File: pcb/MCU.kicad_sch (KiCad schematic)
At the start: 22 parts, among them J2 TC2030, J3 Conn_01x02_Pin, U6 FM24C64B, U7 STM32H563VITx, Y1 3225-25M-SR

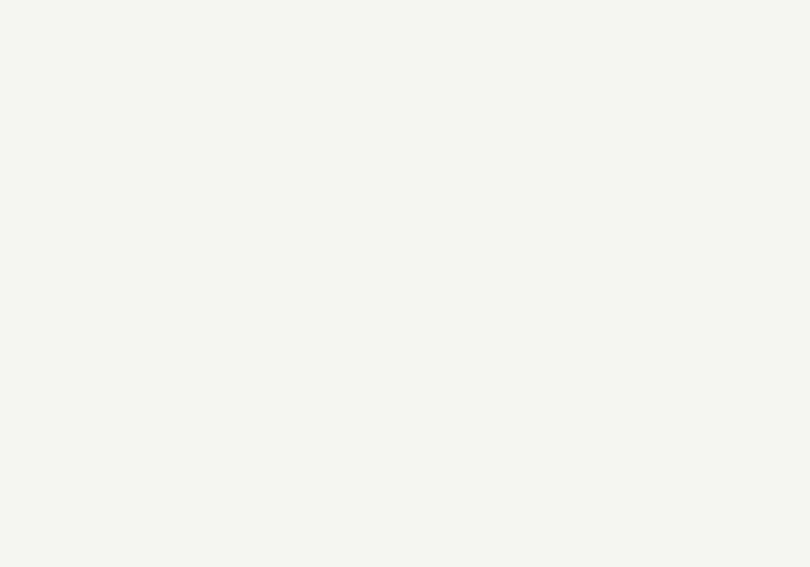
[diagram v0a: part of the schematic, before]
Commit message: Add UniConnector for io expansion (2.0mm pinheader)
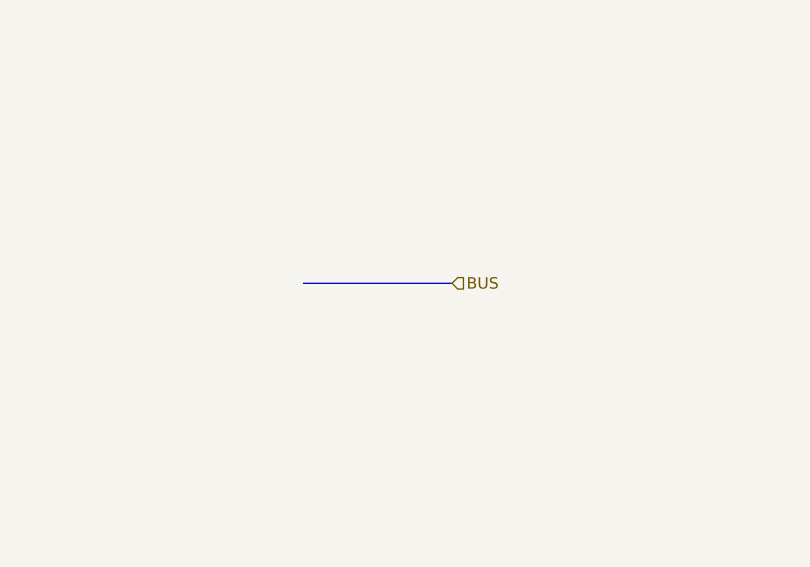
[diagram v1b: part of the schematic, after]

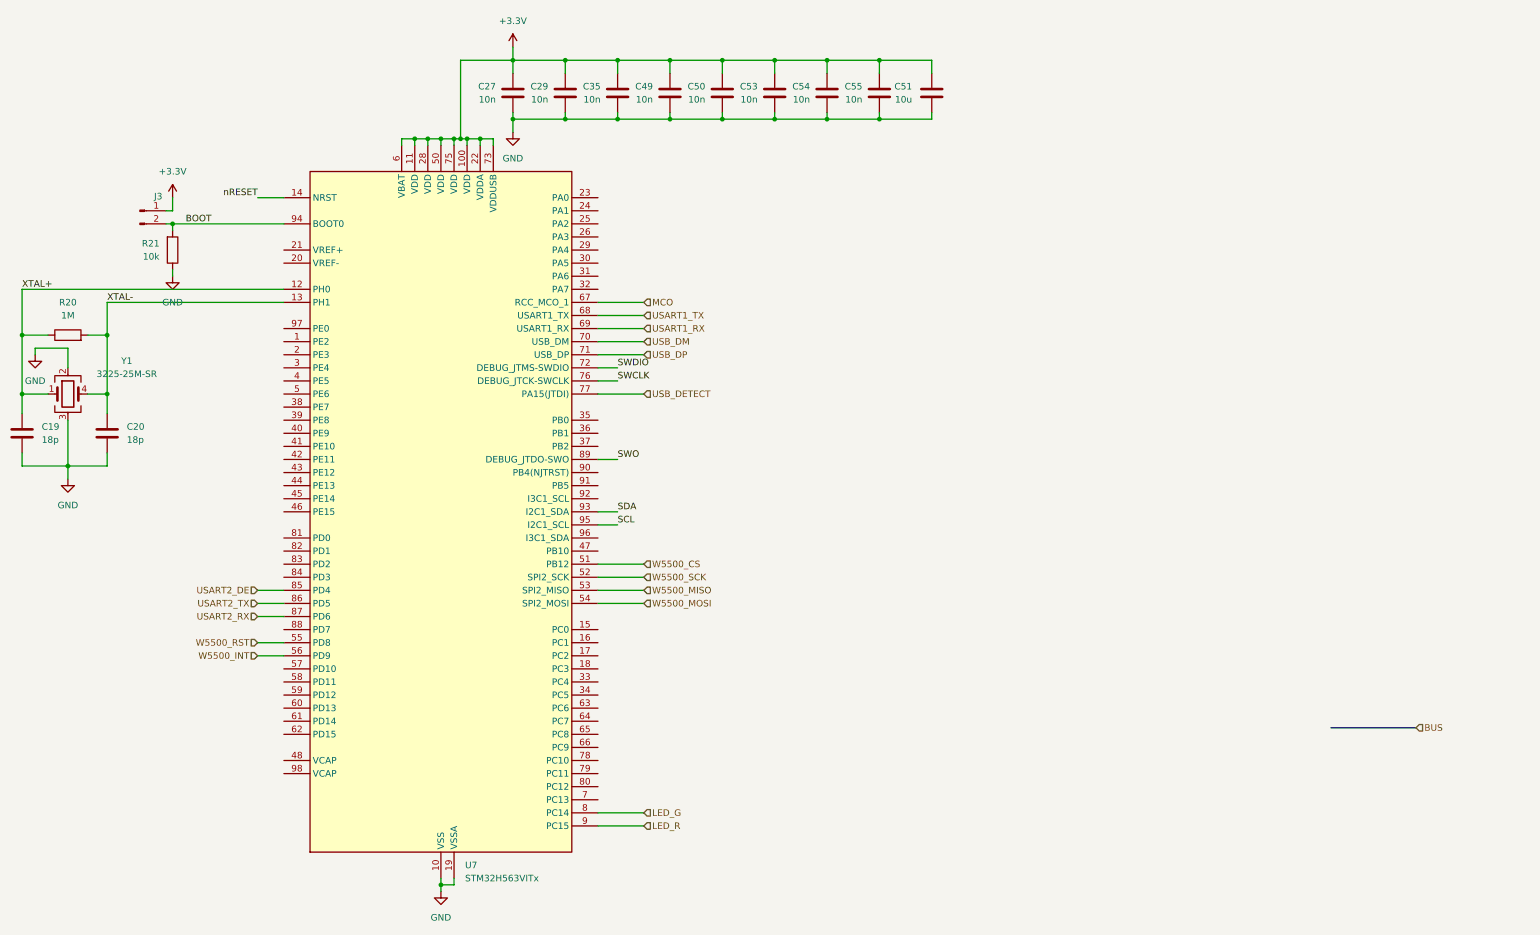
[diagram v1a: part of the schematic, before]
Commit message: Add junction and bus entries to UniConnector schematic
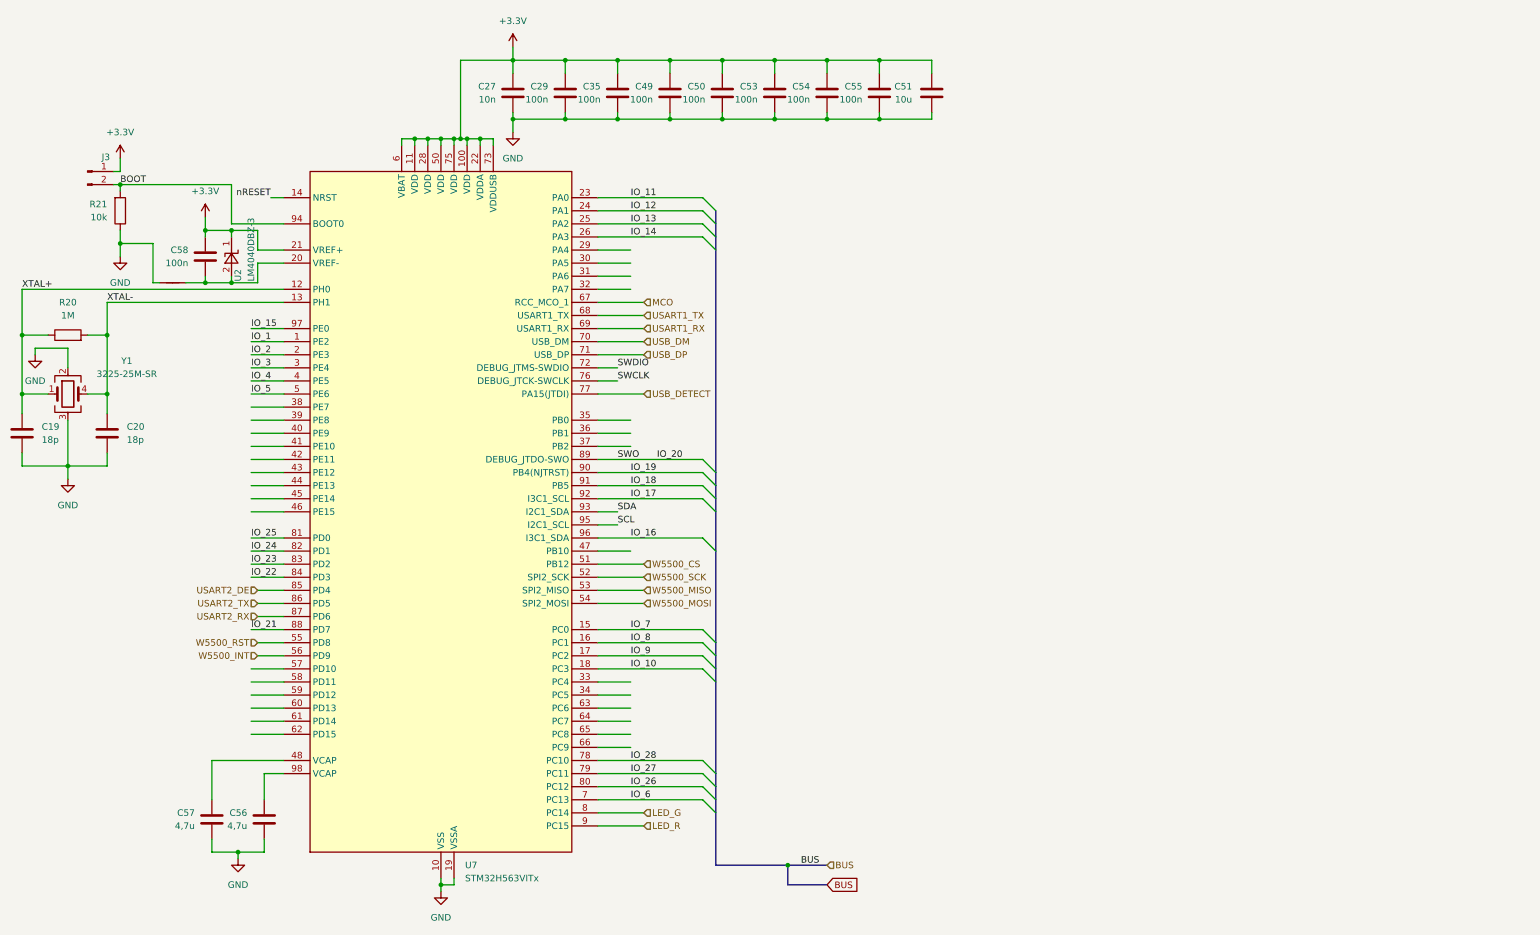
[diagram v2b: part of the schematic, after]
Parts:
- added C56, C57: 4,7u, Capacitor_SMD:C_0603_1608Metric_Pad1.08x0.95mm_HandSolder, symbol Device:C
- added C58: 100n, Capacitor_SMD:C_0603_1608Metric_Pad1.08x0.95mm_HandSolder, symbol Device:C
- added NT1: NetTie_2, NetTie:NetTie-2_SMD_Pad0.5mm, symbol Device:NetTie_2
- added U2: LM4040DBZ-3, Package_TO_SOT_SMD:SOT-23_Handsoldering, symbol Reference_Voltage:LM4040DBZ-3
- C29, C35, C49, C50, C53, C54, C55: value 10n -> 100n
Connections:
- net +3.3V: now also U7.21 (VREF+), C58.2, U2.1 (K)
- net GND: now also C56.1, C57.1, NT1.1
- net IO_1: now reaches U7.1 (PE2)
- net IO_7: now reaches U7.15 (PC0)
- net IO_8: now reaches U7.16 (PC1)
- net IO_9: now reaches U7.17 (PC2)
- net IO_10: now reaches U7.18 (PC3)
- net IO_2: now reaches U7.2 (PE3)
- net at U7.20 (VREF-): now also C58.1, NT1.2, U2.2 (A)
- net IO_11: now reaches U7.23 (PA0)
- net IO_12: now reaches U7.24 (PA1)
- net IO_13: now reaches U7.25 (PA2)
- net IO_14: now reaches U7.26 (PA3)
- net IO_3: now reaches U7.3 (PE4)
- net IO_4: now reaches U7.4 (PE5)
- net at U7.48 (VCAP): now also C57.2
- net IO_5: now reaches U7.5 (PE6)
- net IO_6: now reaches U7.7 (PC13)
- net IO_28: now reaches U7.78 (PC10)
- net IO_27: now reaches U7.79 (PC11)
- net IO_26: now reaches U7.80 (PC12)
- net IO_25: now reaches U7.81 (PD0)
- net IO_24: now reaches U7.82 (PD1)
- net IO_23: now reaches U7.83 (PD2)
- net IO_22: now reaches U7.84 (PD3)
- net IO_21: now reaches U7.88 (PD7)
- net IO_19: now reaches U7.90 (PB4(NJTRST))
- net IO_18: now reaches U7.91 (PB5)
- net IO_17: now reaches U7.92 (PB6)
- net IO_16: now reaches U7.96 (PB9)
- net IO_15: now reaches U7.97 (PE0)
- net at U7.98 (VCAP): now also C56.2
- net SWO renamed IO_20
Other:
- moved on the sheet: J3, R21

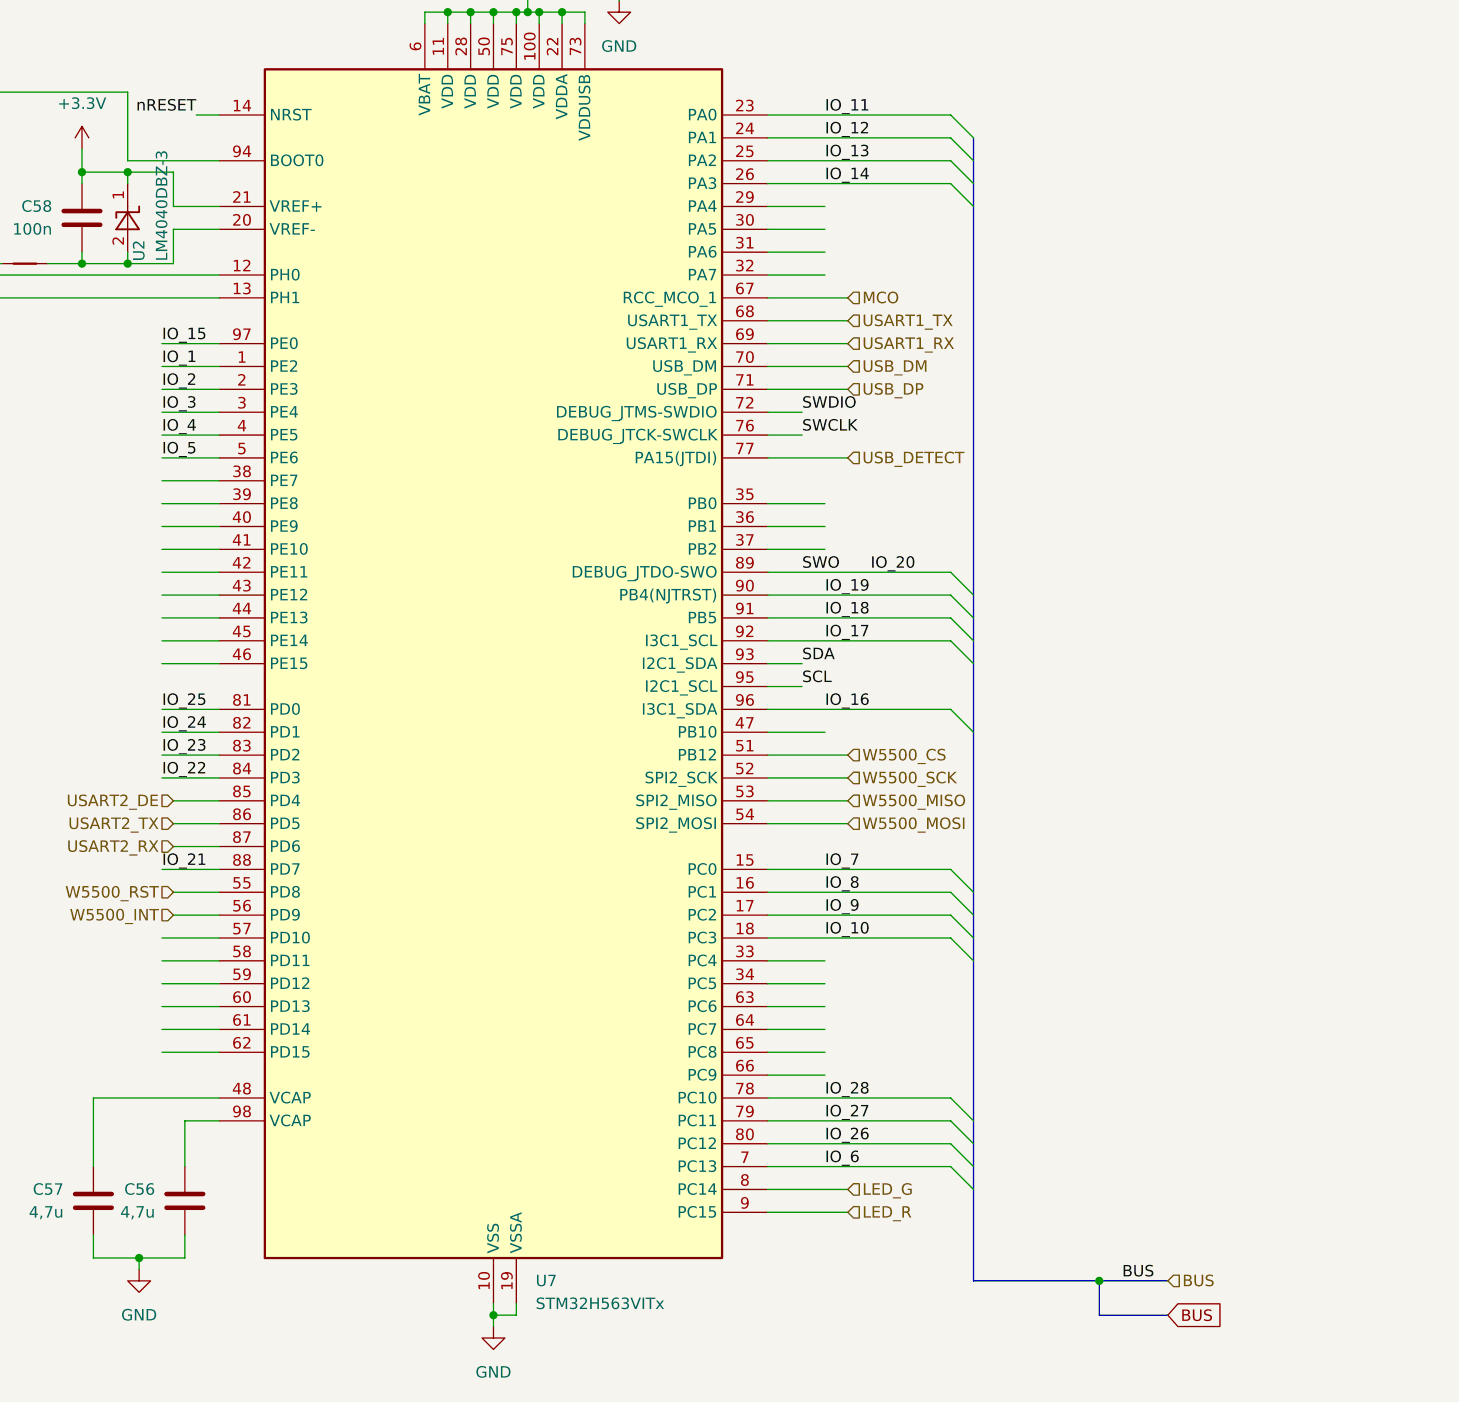
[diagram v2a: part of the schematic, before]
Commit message: UniConnector new traces
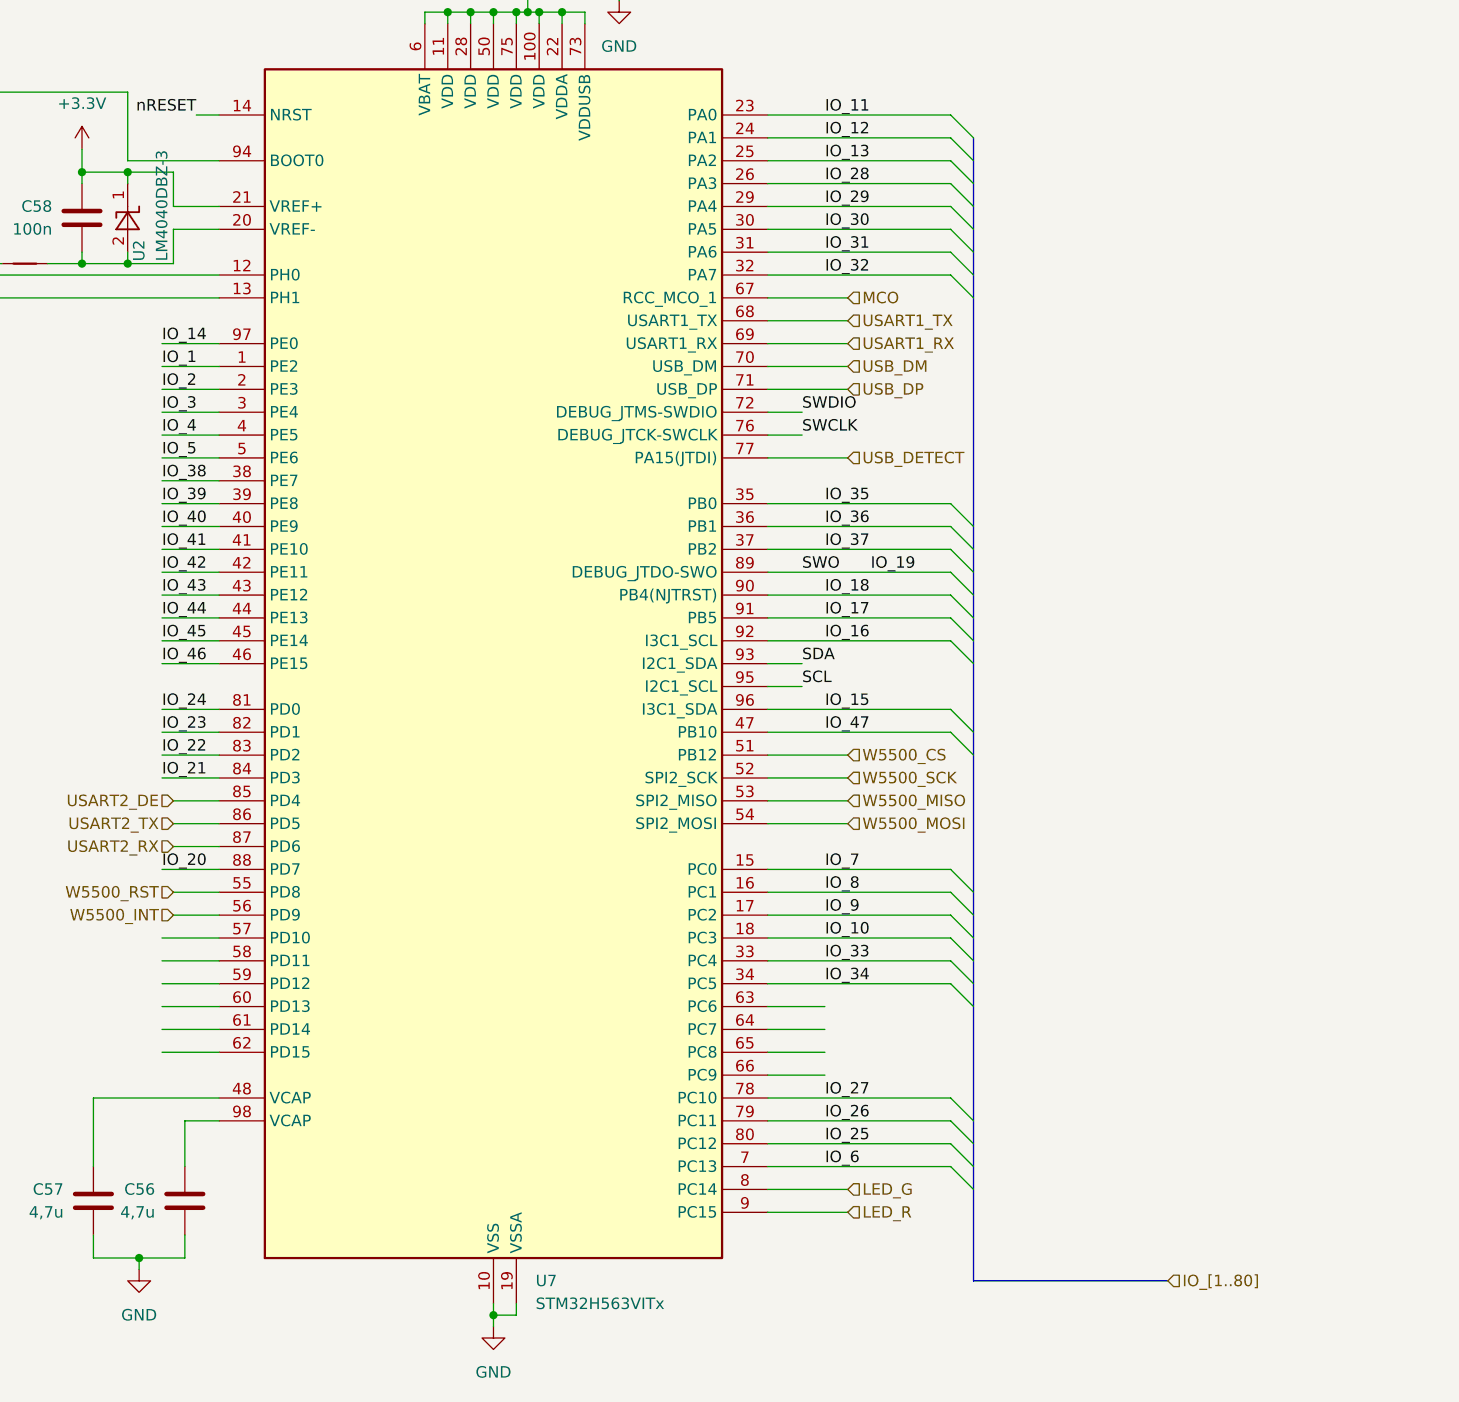
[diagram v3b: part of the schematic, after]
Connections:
- net IO_14: now also U7.97 (PE0); no longer U7.26 (PA3)
- net IO_15: now also U7.96 (PB9); no longer U7.97 (PE0)
- net IO_16: now also U7.92 (PB6); no longer U7.96 (PB9)
- net IO_17: now also U7.91 (PB5); no longer U7.92 (PB6)
- net IO_18: now also U7.90 (PB4(NJTRST)); no longer U7.91 (PB5)
- net IO_19: now also J2.4, U7.89 (PB3(JTDO); no longer U7.90 (PB4(NJTRST))
- net IO_20: now also U7.88 (PD7); no longer J2.4, U7.89 (PB3(JTDO)
- net IO_21: now also U7.84 (PD3); no longer U7.88 (PD7)
- net IO_22: now also U7.83 (PD2); no longer U7.84 (PD3)
- net IO_23: now also U7.82 (PD1); no longer U7.83 (PD2)
- net IO_24: now also U7.81 (PD0); no longer U7.82 (PD1)
- net IO_25: now also U7.80 (PC12); no longer U7.81 (PD0)
- net IO_26: now also U7.79 (PC11); no longer U7.80 (PC12)
- net IO_27: now also U7.78 (PC10); no longer U7.79 (PC11)
- net IO_28: now also U7.26 (PA3); no longer U7.78 (PC10)
- net IO_29: now reaches U7.29 (PA4)
- net IO_30: now reaches U7.30 (PA5)
- net IO_31: now reaches U7.31 (PA6)
- net IO_32: now reaches U7.32 (PA7)
- net IO_33: now reaches U7.33 (PC4)
- net IO_34: now reaches U7.34 (PC5)
- net IO_35: now reaches U7.35 (PB0)
- net IO_36: now reaches U7.36 (PB1)
- net IO_37: now reaches U7.37 (PB2)
- net IO_38: now reaches U7.38 (PE7)
- net IO_39: now reaches U7.39 (PE8)
- net IO_40: now reaches U7.40 (PE9)
- net IO_41: now reaches U7.41 (PE10)
- net IO_42: now reaches U7.42 (PE11)
- net IO_43: now reaches U7.43 (PE12)
- net IO_44: now reaches U7.44 (PE13)
- net IO_45: now reaches U7.45 (PE14)
- net IO_46: now reaches U7.46 (PE15)
- net IO_47: now reaches U7.47 (PB10)
